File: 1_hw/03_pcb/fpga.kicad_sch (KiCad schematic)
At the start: 1 part, among them U2 ICE40UP5K-SG48ITR

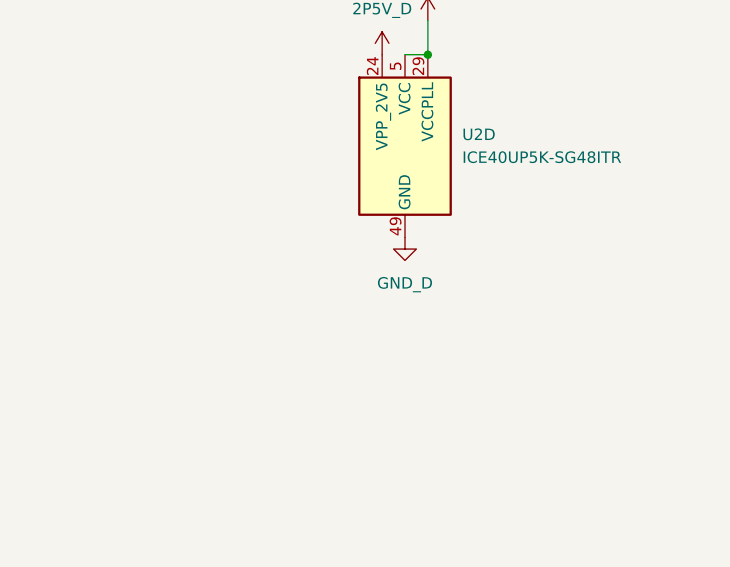
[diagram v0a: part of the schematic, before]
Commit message: FEAT: Changed from two grounds (Digital + Analog) to Singular Ground IAW recommended Grounding Scheme.
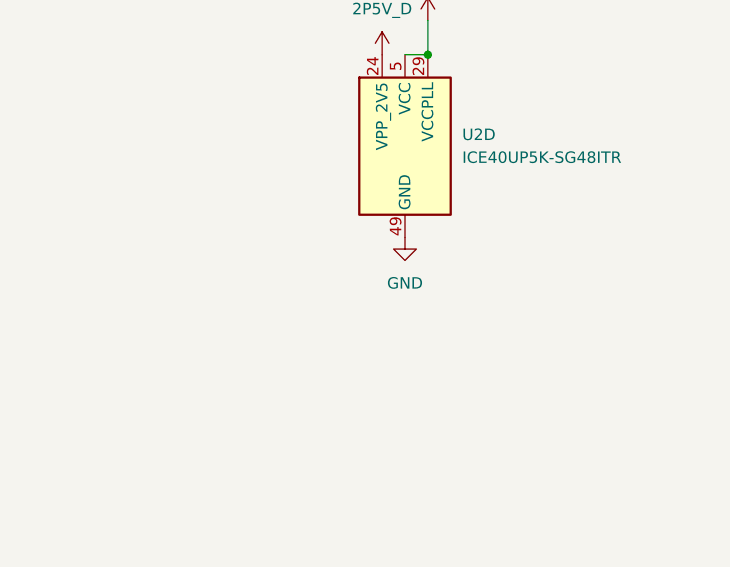
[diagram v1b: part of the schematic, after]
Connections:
- net GND_D renamed GND
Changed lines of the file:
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@@
 			)
 		)
-		(property "Value" "GND_D"
+		(property "Value" "GND"
 			(at 180.34 130.81 0)
 			(effects

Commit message: FEAT: Added MCU Resources for Analog Muxing, Additional DAC, ADC, and I2C for Digital Pot. Also changed SPI Resource from 1 to 2.
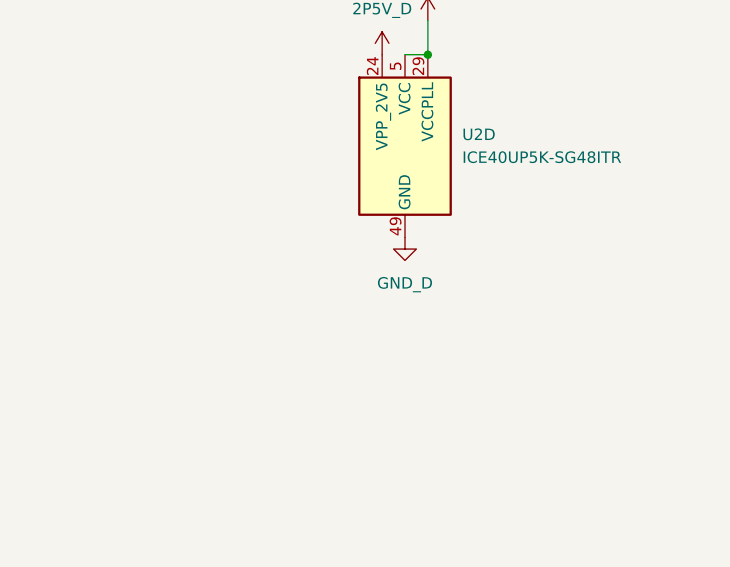
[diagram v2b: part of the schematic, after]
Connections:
- net GND renamed GND_D
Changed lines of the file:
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@@
 			)
 		)
-		(property "Value" "GND"
+		(property "Value" "GND_D"
 			(at 180.34 130.81 0)
 			(effects
